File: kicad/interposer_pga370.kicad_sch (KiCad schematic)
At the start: 45 parts, among them U1 PGA370

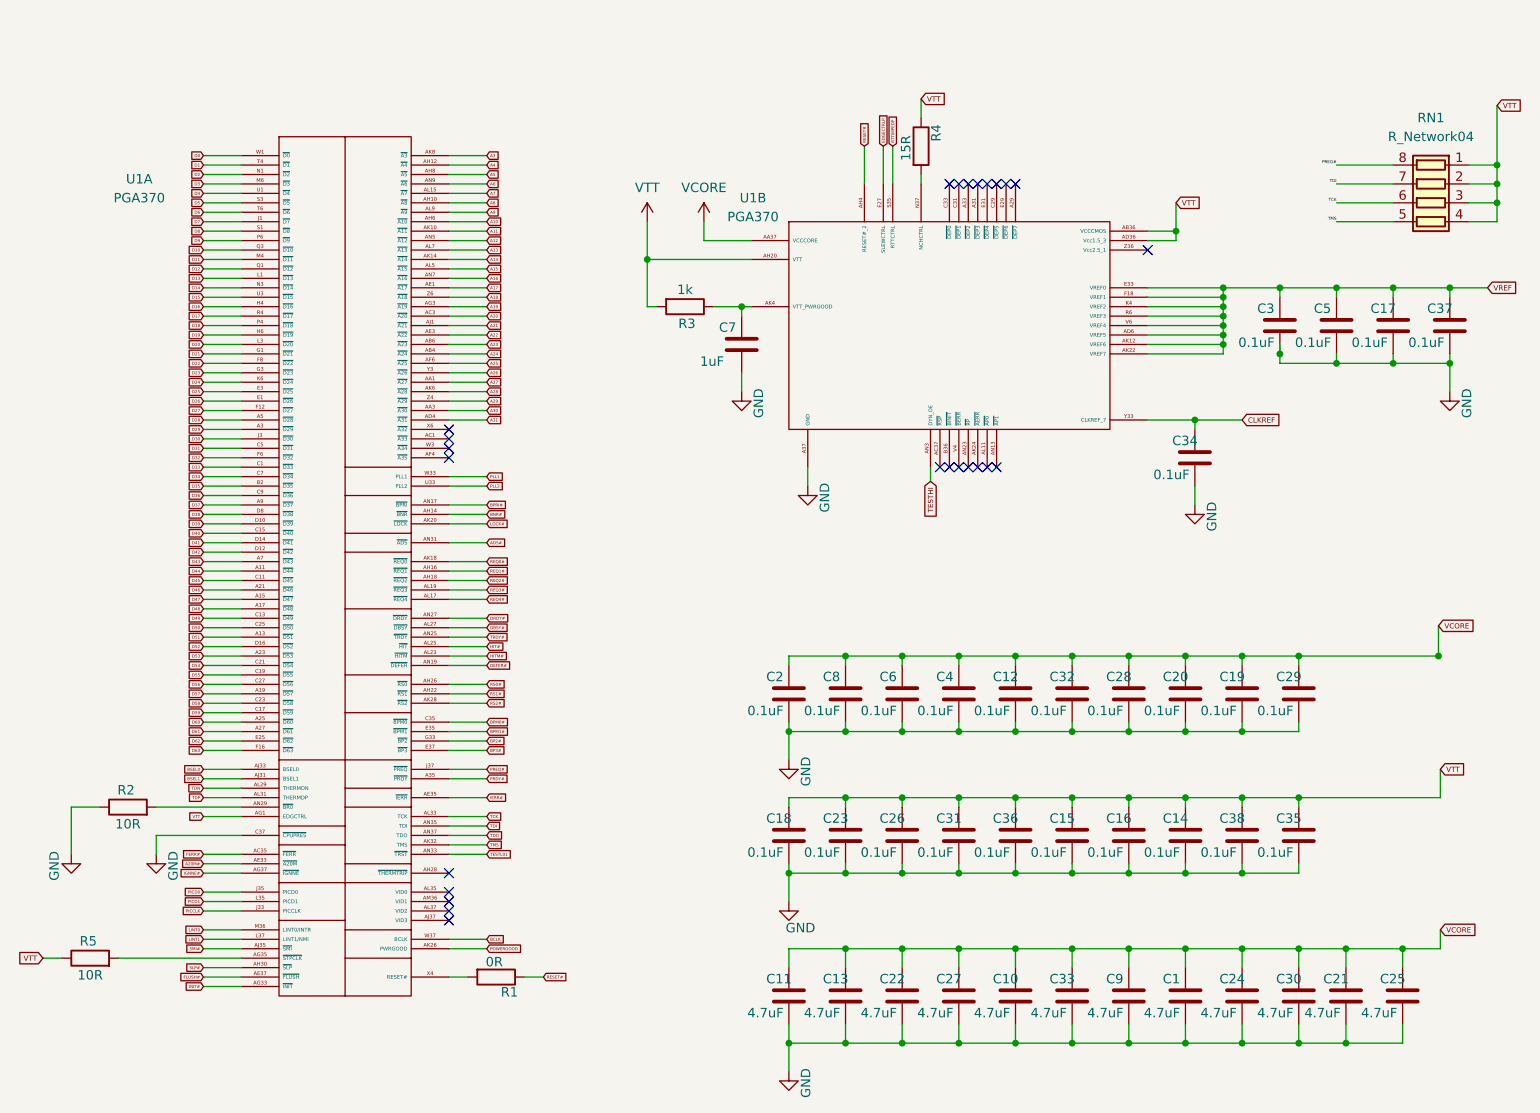
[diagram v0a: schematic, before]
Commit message: Reroute with BGA more centered and cheaper design fabrications (0.3mm drills).
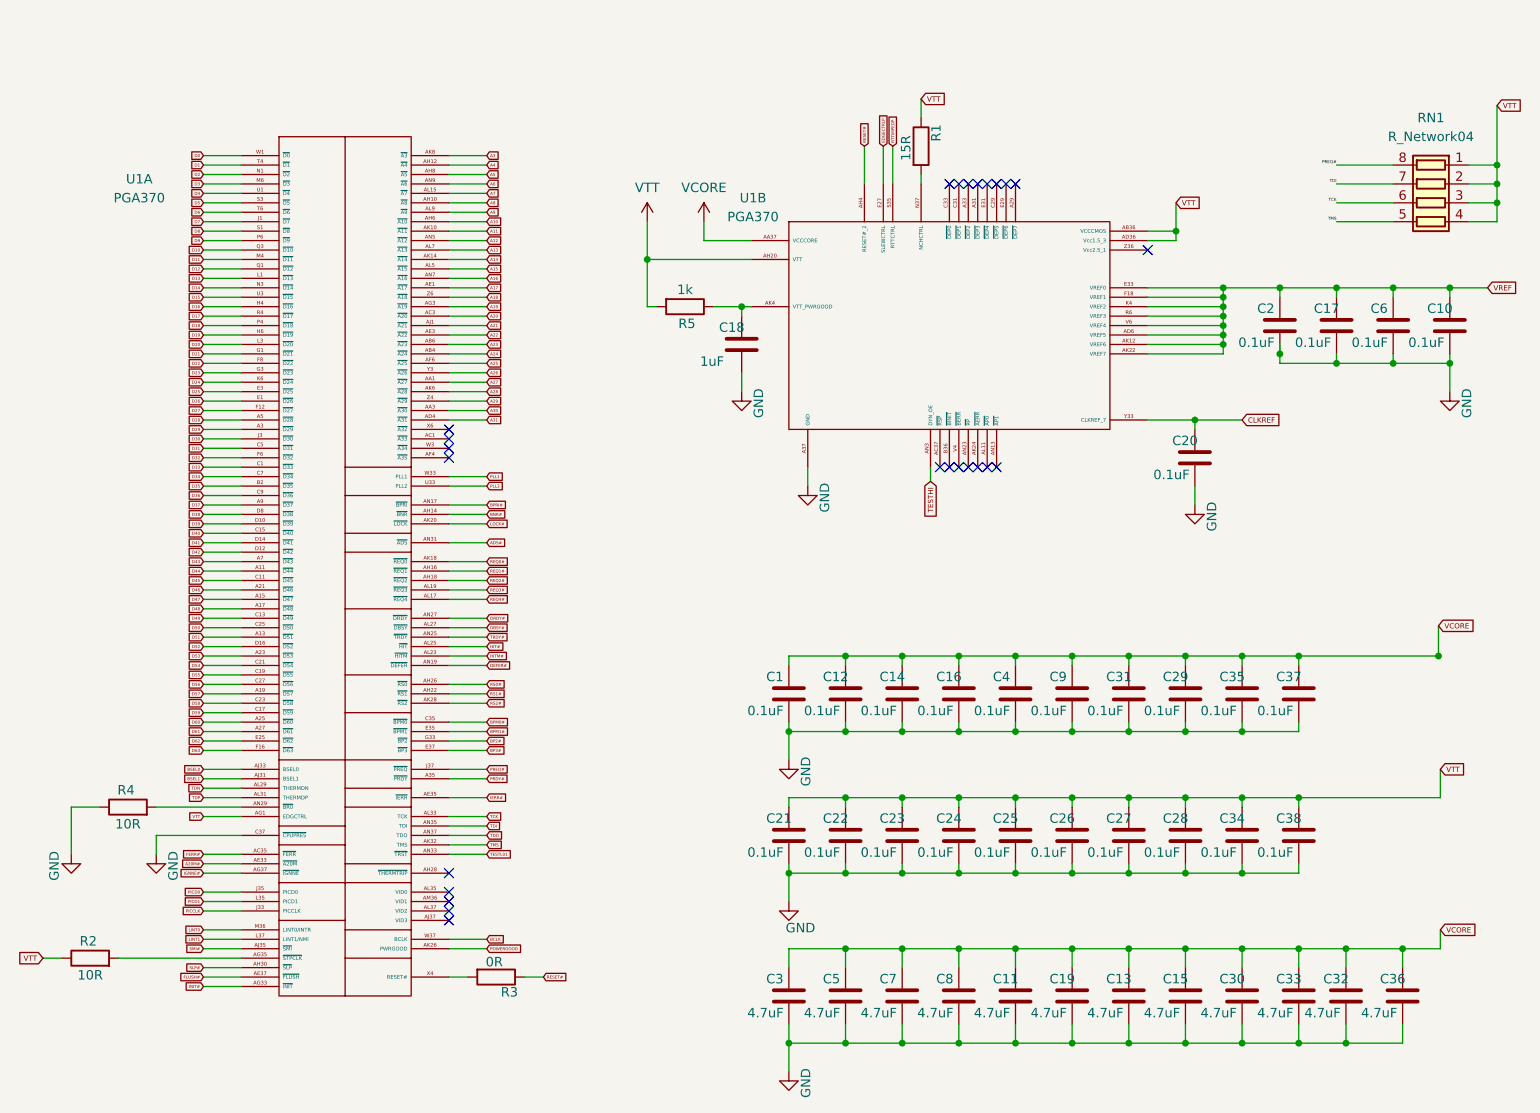
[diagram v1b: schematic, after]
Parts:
- renumbered C2 to C1, C37 to C10, C10 to C11, C8 to C12, C9 to C13, C6 to C14, C1 to C15, C4 to C16, C5 to C17, C7 to C18, C33 to C19, C3 to C2, C34 to C20, C18 to C21, C23 to C22, C26 to C23, C31 to C24, C36 to C25, C15 to C26, C16 to C27, C14 to C28, C20 to C29, C11 to C3, C24 to C30, C28 to C31, C21 to C32, C30 to C33, C38 to C34, C19 to C35, C25 to C36, C29 to C37, C35 to C38, C12 to C4, C13 to C5, C17 to C6, C22 to C7, C27 to C8, C32 to C9, R4 to R1, R5 to R2, R1 to R3, R2 to R4, R3 to R5

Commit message: Revision 3; much cleaner layout with traces tuned to 25mm.
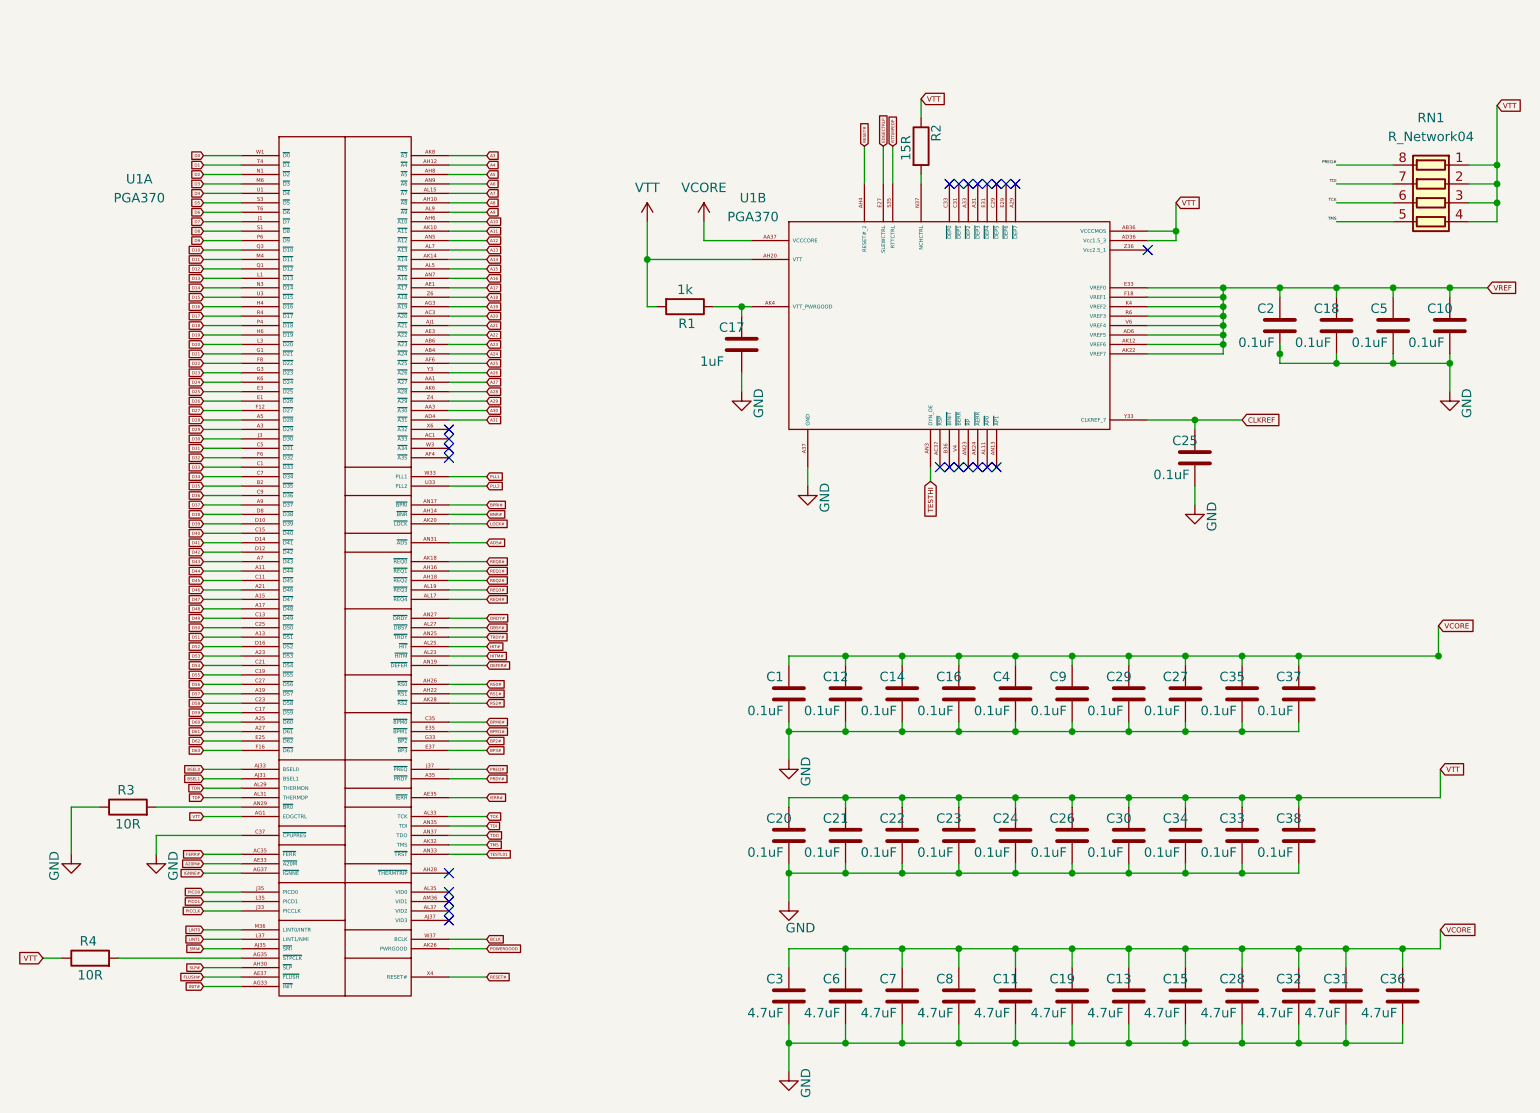
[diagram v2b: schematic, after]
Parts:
- removed R3: 0R, Resistor_SMD:R_0603_1608Metric, symbol Device:R
- renumbered C18 to C17, C17 to C18, C21 to C20, C22 to C21, C23 to C22, C24 to C23, C25 to C24, C20 to C25, C29 to C27, C30 to C28, C31 to C29, C27 to C30, C32 to C31, C33 to C32, C34 to C33, C28 to C34, C6 to C5, C5 to C6, R5 to R1, R1 to R2, R4 to R3, R2 to R4
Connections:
- net RESET#: now also U1.X4 (RESET#)

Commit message: Revision 3.2
Implement fixes that allow interposer to be actually functional for the first time:
 - Fix uBGA495 pin P1 from VTT --> VCC since this is VCC on xbox motherboard.
 - Fix P370 pin AJ3 (RESET2#) from GND --> NC.

Furthermore, pins AL1 (reserved), AK36 (VID output), AF36 (DETECT) now left NC instead of connected to GND.

Outline slightly trimmed near bottom to provide some clearance against a cap on 1.6 motherboards.

Design specs loosened, from 4 mil tracks/4 mil clearance/0.3mm drills --> 5 mil/5 mil/0.3mm.

Board thickness recommendation is now 1.6mm instead of 1.2mm for additional rigidity.
Trace lengths now matched at 27.0mm (was 25.0mm).

Added BGA footprint indicator on front silkscreen.
Added BGA pin numbering on back silkscreen.
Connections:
- net GND: no longer U1.AF36 (GND), U1.AJ3 (GND), U1.AK36 (GND), U1.AL1 (GND)
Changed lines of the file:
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@@
     (pin "AF32")
     (pin "AF34")
-    (pin "AF36")
     (pin "AG5")
     (pin "AH2")
@@
     (pin "AJ27")
     (pin "AJ29")
-    (pin "AJ3")
     (pin "AJ5")
     (pin "AJ7")
@@
     (pin "AK24")
     (pin "AK34")
-    (pin "AK36")
     (pin "AK4")
-    (pin "AL1")
     (pin "AL11")
     (pin "AL13")
@@
     (pin "AF32")
     (pin "AF34")
-    (pin "AF36")
     (pin "AG5")
     (pin "AH2")
@@
     (pin "AJ27")
     (pin "AJ29")
-    (pin "AJ3")
     (pin "AJ5")
     (pin "AJ7")
@@
     (pin "AK24")
     (pin "AK34")
-    (pin "AK36")
     (pin "AK4")
-    (pin "AL1")
     (pin "AL11")
     (pin "AL13")

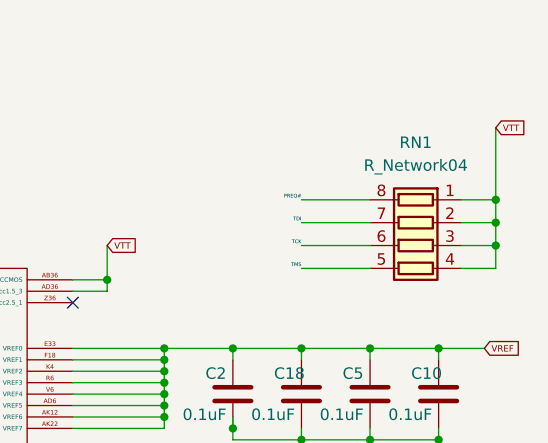
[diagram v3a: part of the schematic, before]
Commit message: Rev. 3.3, minor changes:  - Resistor network RN01 changed to 4 distinct 0603's since people continuously order an incorrect part  - Height of interposer slightly reduced by 0.3mm on both top and bottom. on top, the pins for standard mounting bracket require less trimming. On bottom there is less obstruction with C1D5 on xbox motherboard.  - Added xbox.munia.io branding on the bottom silk  - Align tool modified accordingly.
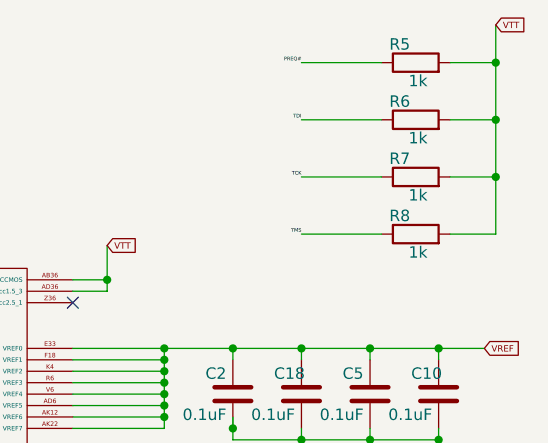
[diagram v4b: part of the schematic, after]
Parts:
- removed RN1: R_Network04, Resistor_SMD:R_Array_Concave_4x0603, symbol Device:R_Pack04
- added R5, R6, R7, R8: 1k, Resistor_SMD:R_0603_1608Metric, symbol Device:R
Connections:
- net PREQ#: now also R5.1
- net TCK: now also R7.1
- net TDI: now also R6.1
- net TMS: now also R8.1
- net VTT: now also R5.2, R6.2, R7.2, R8.2
